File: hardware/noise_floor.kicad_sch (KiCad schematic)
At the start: 10 parts, among them J1 Input, J2 Output, J3 DC Power, J4 IO/Effect Connector 1 (IO Sid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, J5 IO/Effect Connector 2 (IO Sid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, J6 IO/Switch Connector 1 (IO Sid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, J7 IO/Switch Connector 2 (IO Sid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, J8 IO/Switch Connector 1 (Switch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, J9 IO/Switch Connector 2 (Switch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, SW1 Footswitch

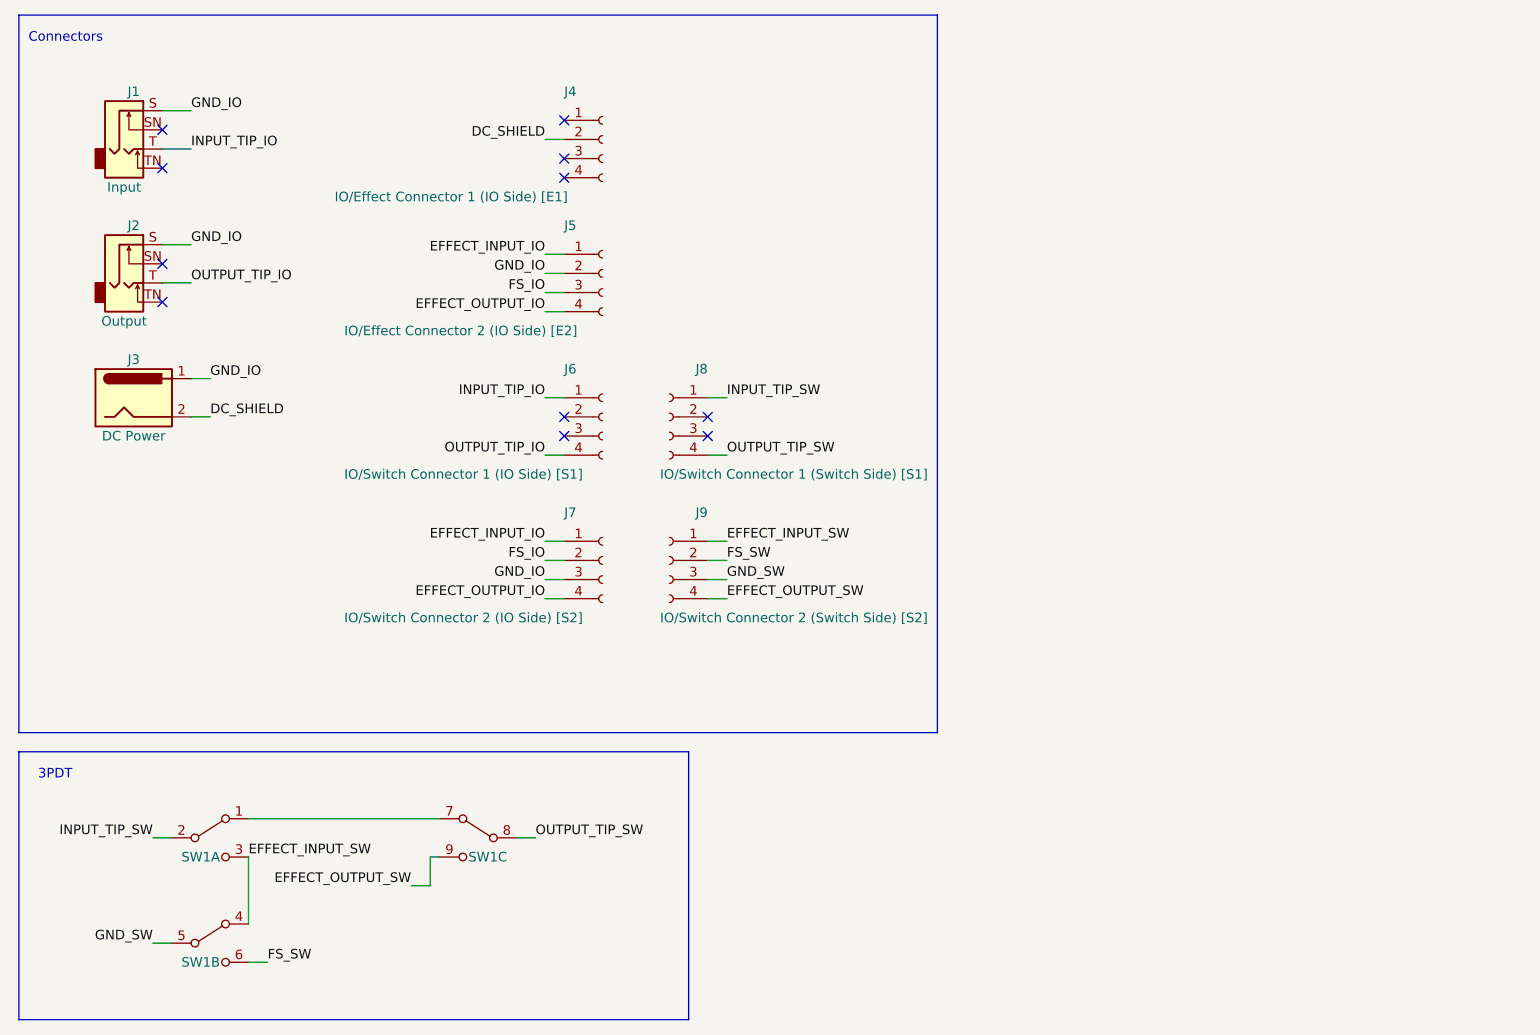
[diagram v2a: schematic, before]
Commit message: Offload DC protection and LED indicator to "noise floor" utility boards
 - much rerouting and layout work, but functionally the same
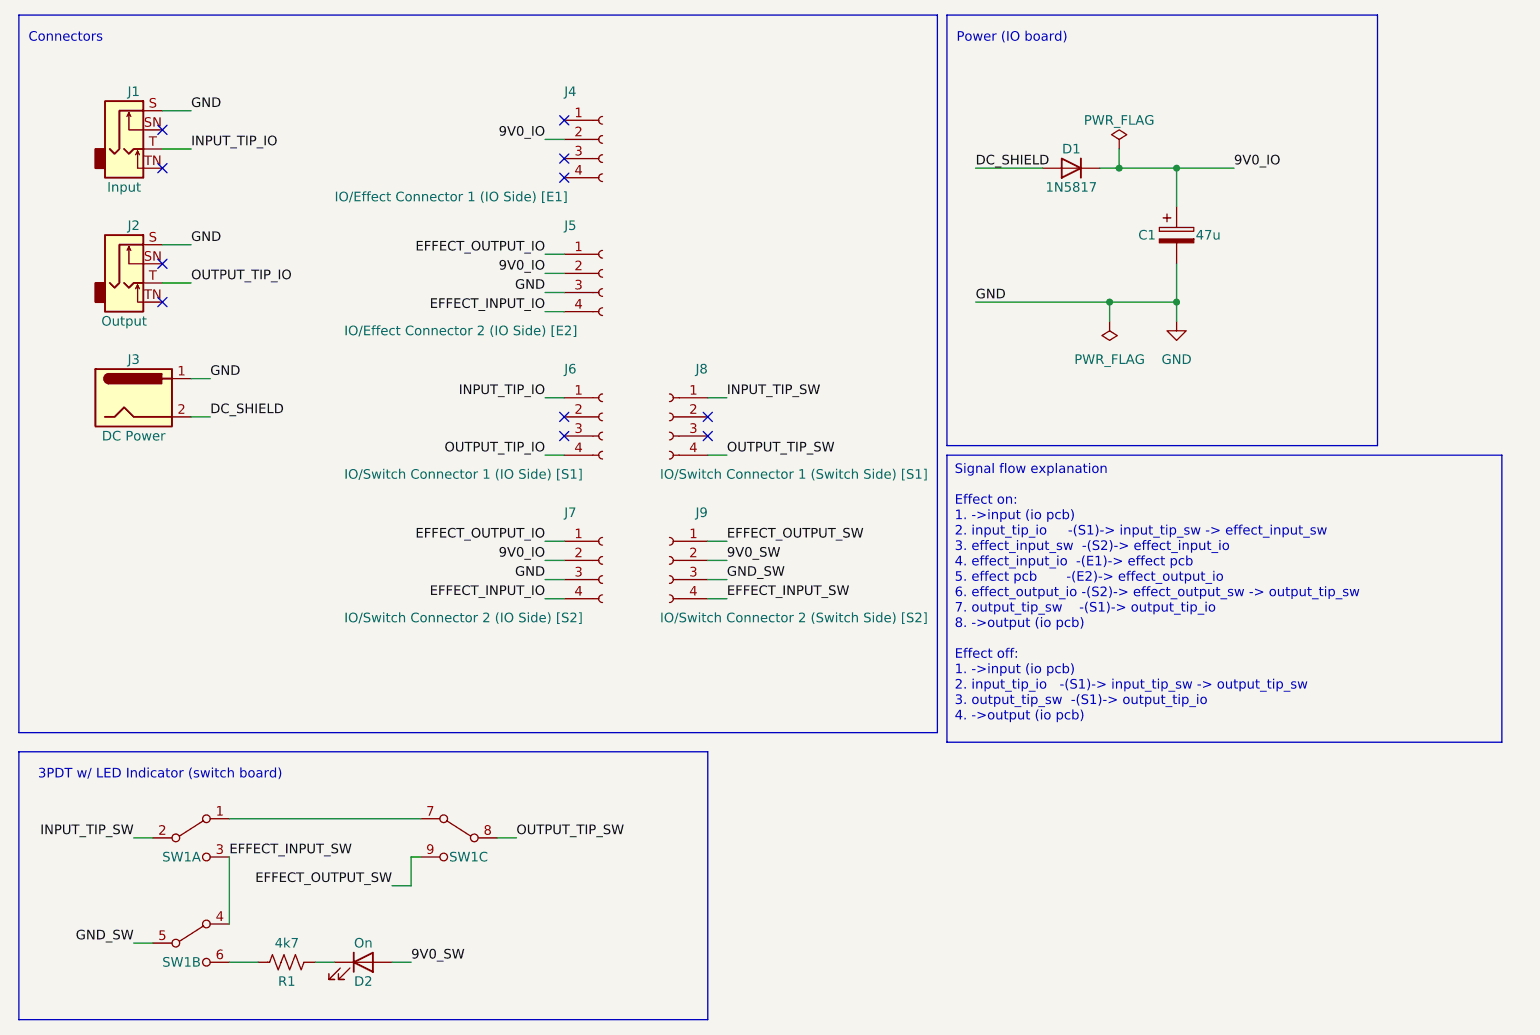
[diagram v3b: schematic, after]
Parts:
- added C1: 47u, Capacitor_THT:CP_Radial_D5.0mm_P2.50mm, symbol Device:C_Polarized
- added D1: 1N5817, Diode_THT:D_DO-35_SOD27_P7.62mm_Horizontal, symbol Device:D
- added D2: On, LED_THT:LED_D3.0mm, symbol Device:LED
- added R1: 4k7, Resistor_THT:R_Axial_DIN0207_L6.3mm_D2.5mm_P7.62mm_Horizontal, symbol Device:R_US
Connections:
- net DC_SHIELD: now also D1.2 (A); no longer J4.2 (Pin_2)
- net EFFECT_INPUT_IO: now also J5.4 (Pin_4), J7.4 (Pin_4); no longer J5.1 (Pin_1), J7.1 (Pin_1)
- net EFFECT_INPUT_SW: now also J9.4 (Pin_4); no longer J9.1 (Pin_1)
- net EFFECT_OUTPUT_IO: now also J5.1 (Pin_1), J7.1 (Pin_1); no longer J5.4 (Pin_4), J7.4 (Pin_4)
- net EFFECT_OUTPUT_SW: now also J9.1 (Pin_1); no longer J9.4 (Pin_4)
- net FS_IO renamed 9V0_IO
- net 9V0_IO: now also J4.2 (Pin_2), J5.2 (Pin_2), C1.1, D1.1 (K); no longer J5.3 (Pin_3)
- net FS_SW: no longer names the net of SW1.6 (B3)
- net FS_SW: now also R1.2; no longer J9.2 (Pin_2)
- net GND_IO renamed GND
- net GND: now also J5.3 (Pin_3), C1.2; no longer J5.2 (Pin_2)
- new net: D2.1 (K), R1.1
- new net 9V0_SW: D2.2 (A), J9.2 (Pin_2)
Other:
- note added: "3PDT w/ LED Indicator (switch board)"
- note added: "Power (IO board)"
- note removed: "3PDT"
- moved on the sheet: SW1A, SW1B, SW1C
